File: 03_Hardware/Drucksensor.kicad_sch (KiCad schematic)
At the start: 85 parts, among them J101 24V in, J103 RS485-mini-1, J104 RJ45, J108 RJ45, J109 RJ45, J110 DS18B20, J111 BMP280, J112 RJ45, J113 RS485-mini-1, J114 AVR-ISP-6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

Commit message: Curve Fit Algo auf Spannungsteiler Detektion Sensor geworfen => 18,8k kamen raus. Jetzt wird es mal mit 18k probiert.
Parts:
- R111, R137: value 33k -> 18k
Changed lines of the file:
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@@
       (effects (font (size 1.27 1.27)))
     )
-    (property "Value" "33k" (at 312.42 43.18 90)
+    (property "Value" "18k" (at 312.42 43.18 90)
       (effects (font (size 1.27 1.27)))
     )
@@
       (effects (font (size 1.27 1.27)))
     )
-    (property "Value" "33k" (at 312.42 97.79 90)
-      (effects (font (size 1.27 1.27)))
-    )
+    (property "Value" "18k" (at 312.42 97.79 90)
+      (effects (font (size 1.27 1.27)))
+    )

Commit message: BiDir 5V TVS Diode an ID Leitung Sensor angebracht
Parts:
- added D1, D2: SD05_SOD323, Diode_SMD:D_SOD-323, symbol Diode:SD05_SOD323
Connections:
- net ADC0_ID_1: now also D1.2 (A2)
- net ADC1_ID_2: now also D2.2 (A2)
- net GND: now also D1.1 (A1), D2.1 (A1)
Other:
- note removed: "ESD-Schutz an ID-Widerstandsmessungen fehlen!"
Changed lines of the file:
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@@
   (junction (at 120.65 59.69) (diameter 0) (color 0 0 0 0)
   )
+  (junction (at 317.5 90.17) (diameter 0) (color 0 0 0 0)
+  )
   (junction (at 93.98 36.83) (diameter 0) (color 0 0 0 0)
   )
@@
   (junction (at 276.86 257.81) (diameter 0) (color 0 0 0 0)
   )
+  (junction (at 317.5 35.56) (diameter 0) (color 0 0 0 0)
+  )
   (junction (at 368.3 172.72) (diameter 0) (color 0 0 0 0)
   )
@@
     (stroke (width 0) (type solid))
   )
+  (wire (pts (xy 317.5 87.63) (xy 317.5 90.17))
+    (stroke (width 0) (type default))
+  )
   (wire (pts (xy 119.38 72.39) (xy 120.65 72.39))
     (stroke (width 0) (type default))
@@
     (stroke (width 0) (type solid))
   )
+  (wire (pts (xy 317.5 31.75) (xy 317.5 35.56))
+    (stroke (width 0) (type default))
+  )
   (wire (pts (xy 276.86 234.95) (xy 276.86 245.11))
     (stroke (width 0) (type default))
@@
     (stroke (width 0) (type default))
   )
-  (text "ESD-Schutz an ID-Widerstandsmessungen fehlen!" (at 217.17 77.47 0)
-    (effects (font (size 2.5 2.5) (thickness 0.5) bold (color 221 38 8 1)) (justify left bottom))
-  )
   (text "Messröhre ADC:\nVon Röhre 0-10V\nTeiler 20k:13.895k (33.895k R-ges)\nErgibt Teilerverhältnis von 0,40995\nBei idealem Teilerverhältnis von 0,4096\n"
     (at 361.95 124.46 0)
@@
     )
   )
+  (symbol (lib_id "power:GND") (at 317.5 80.01 0) (mirror x) (unit 1)
+    (in_bom yes) (on_board yes) (dnp no) (fields_autoplaced)
+    (property "Reference" "#PWR01" (at 317.5 73.66 0)
+      (effects (font (size 1.27 1.27)) hide)
+    )
+    (property "Value" "GND" (at 316.865 76.2 90)
+      (effects (font (size 1.27 1.27)) (justify right))
+    )
+    (property "Footprint" "" (at 317.5 80.01 0)
+      (effects (font (size 1.27 1.27)) hide)
+    )
+    (property "Datasheet" "" (at 317.5 80.01 0)
+      (effects (font (size 1.27 1.27)) hide)
+    )
+    (pin "1")
+    (instances
+      (project "Drucksensor"
+        (path "/d772951a-27ae-4d3f-b561-d53c012cef6f"
+          (reference "#PWR01") (unit 1)
+        )
+      )
+    )
+  )
   (symbol (lib_id "power:+5V") (at 165.1 175.26 0) (unit 1)
     (in_bom yes) (on_board yes) (dnp no)
@@
     )
   )
+  (symbol (lib_id "Diode:SD05_SOD323") (at 317.5 27.94 270) (unit 1)
+    (in_bom yes) (on_board yes) (dnp no) (fields_autoplaced)
+    (property "Reference" "D2" (at 322.58 27.94 0)
+      (effects (font (size 1.27 1.27)))
+    )
+    (property "Value" "SD05_SOD323" (at 320.04 27.94 0)
+      (effects (font (size 1.27 1.27)))
+    )
+    (property "Footprint" "Diode_SMD:D_SOD-323" (at 312.42 27.94 0)
+      (effects (font (size 1.27 1.27)) hide)
+    )
+    (property "Datasheet" "https://www.littelfuse.com/~/media/electronics/datasheets/tvs_diode_arrays/littelfuse_tvs_diode_array_sd_c_datasheet.pdf.pdf" (at 317.5 27.94 0)
+      (effects (font (size 1.27 1.27)) hide)
+    )
+    (pin "1")
+    (pin "2")
+    (instances
+      (project "Drucksensor"
+        (path "/d772951a-27ae-4d3f-b561-d53c012cef6f"
+          (reference "D2") (unit 1)
+        )
+      )
+    )
+  )
   (symbol (lib_id "power:+24V") (at 191.77 30.48 90) (mirror x) (unit 1)
     (in_bom yes) (on_board yes) (dnp no)
@@
     )
   )
+  (symbol (lib_id "Diode:SD05_SOD323") (at 317.5 83.82 270) (unit 1)
+    (in_bom yes) (on_board yes) (dnp no) (fields_autoplaced)
+    (property "Reference" "D1" (at 322.58 83.82 0)
+      (effects (font (size 1.27 1.27)))
+    )
+    (property "Value" "SD05_SOD323" (at 320.04 83.82 0)
+      (effects (font (size 1.27 1.27)))
+    )
+    (property "Footprint" "Diode_SMD:D_SOD-323" (at 312.42 83.82 0)
+      (effects (font (size 1.27 1.27)) hide)
+    )
+    (property "Datasheet" "https://www.littelfuse.com/~/media/electronics/datasheets/tvs_diode_arrays/littelfuse_tvs_diode_array_sd_c_datasheet.pdf.pdf" (at 317.5 83.82 0)
+      (effects (font (size 1.27 1.27)) hide)
+    )
+    (pin "1")
+    (pin "2")
+    (instances
+      (project "Drucksensor"
+        (path "/d772951a-27ae-4d3f-b561-d53c012cef6f"
+          (reference "D1") (unit 1)
+        )
+      )
+    )
+  )
   (symbol (lib_id "Device:C") (at 86.36 252.73 0) (unit 1)
     (in_bom yes) (on_board yes) (dnp no) (fields_autoplaced)
@@
         )
       )
+    )
+  )
+  (symbol (lib_id "power:GND") (at 317.5 24.13 0) (mirror x) (unit 1)
+    (in_bom yes) (on_board yes) (dnp no) (fields_autoplaced)
+    (property "Reference" "#PWR02" (at 317.5 17.78 0)
+      (effects (font (size 1.27 1.27)) hide)
+    )
+    (property "Value" "GND" (at 316.865 20.32 90)
+      (effects (font (size 1.27 1.27)) (justify right))
+    )
+    (property "Footprint" "" (at 317.5 24.13 0)
+      (effects (font (size 1.27 1.27)) hide)
+    )
+    (property "Datasheet" "" (at 317.5 24.13 0)
+      (effects (font (size 1.27 1.27)) hide)
+    )
+    (pin "1")
+    (instances
+      (project "Drucksensor"
+        (path "/d772951a-27ae-4d3f-b561-d53c012cef6f"
+          (reference "#PWR02") (unit 1)
+        )
+      )

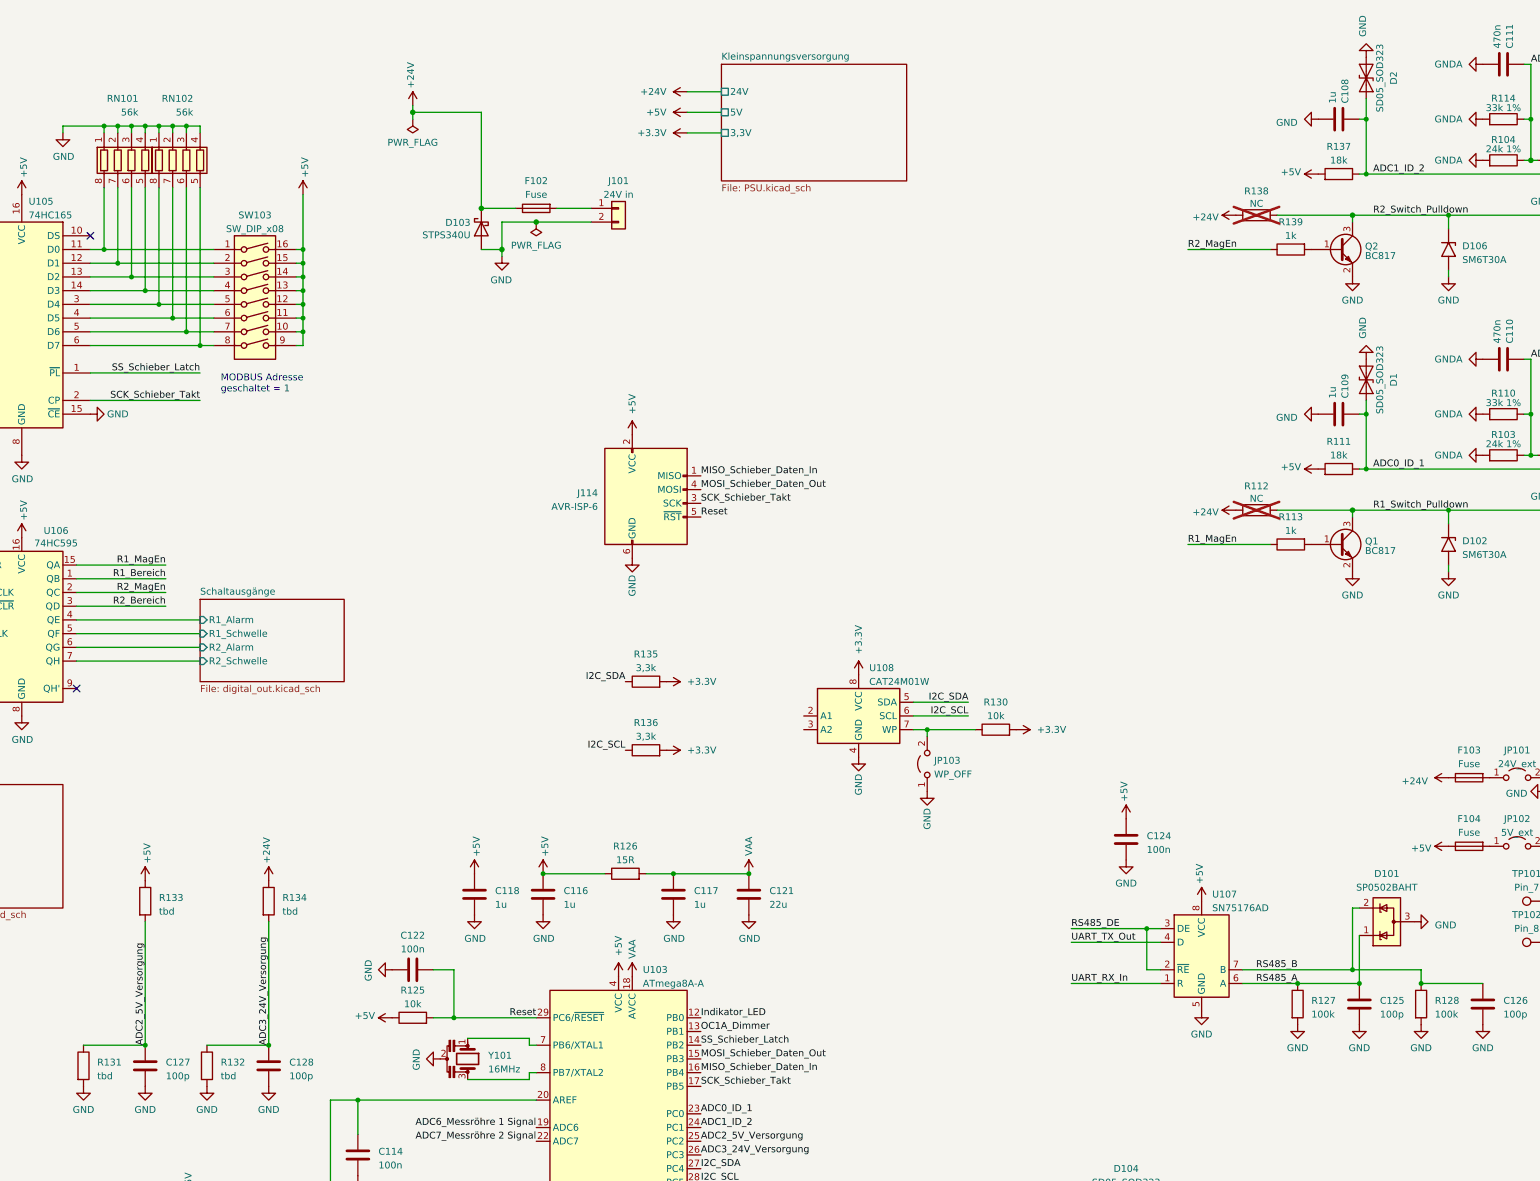
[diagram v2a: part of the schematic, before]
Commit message: Software angefangen - vscode und Platformio, mega328pb
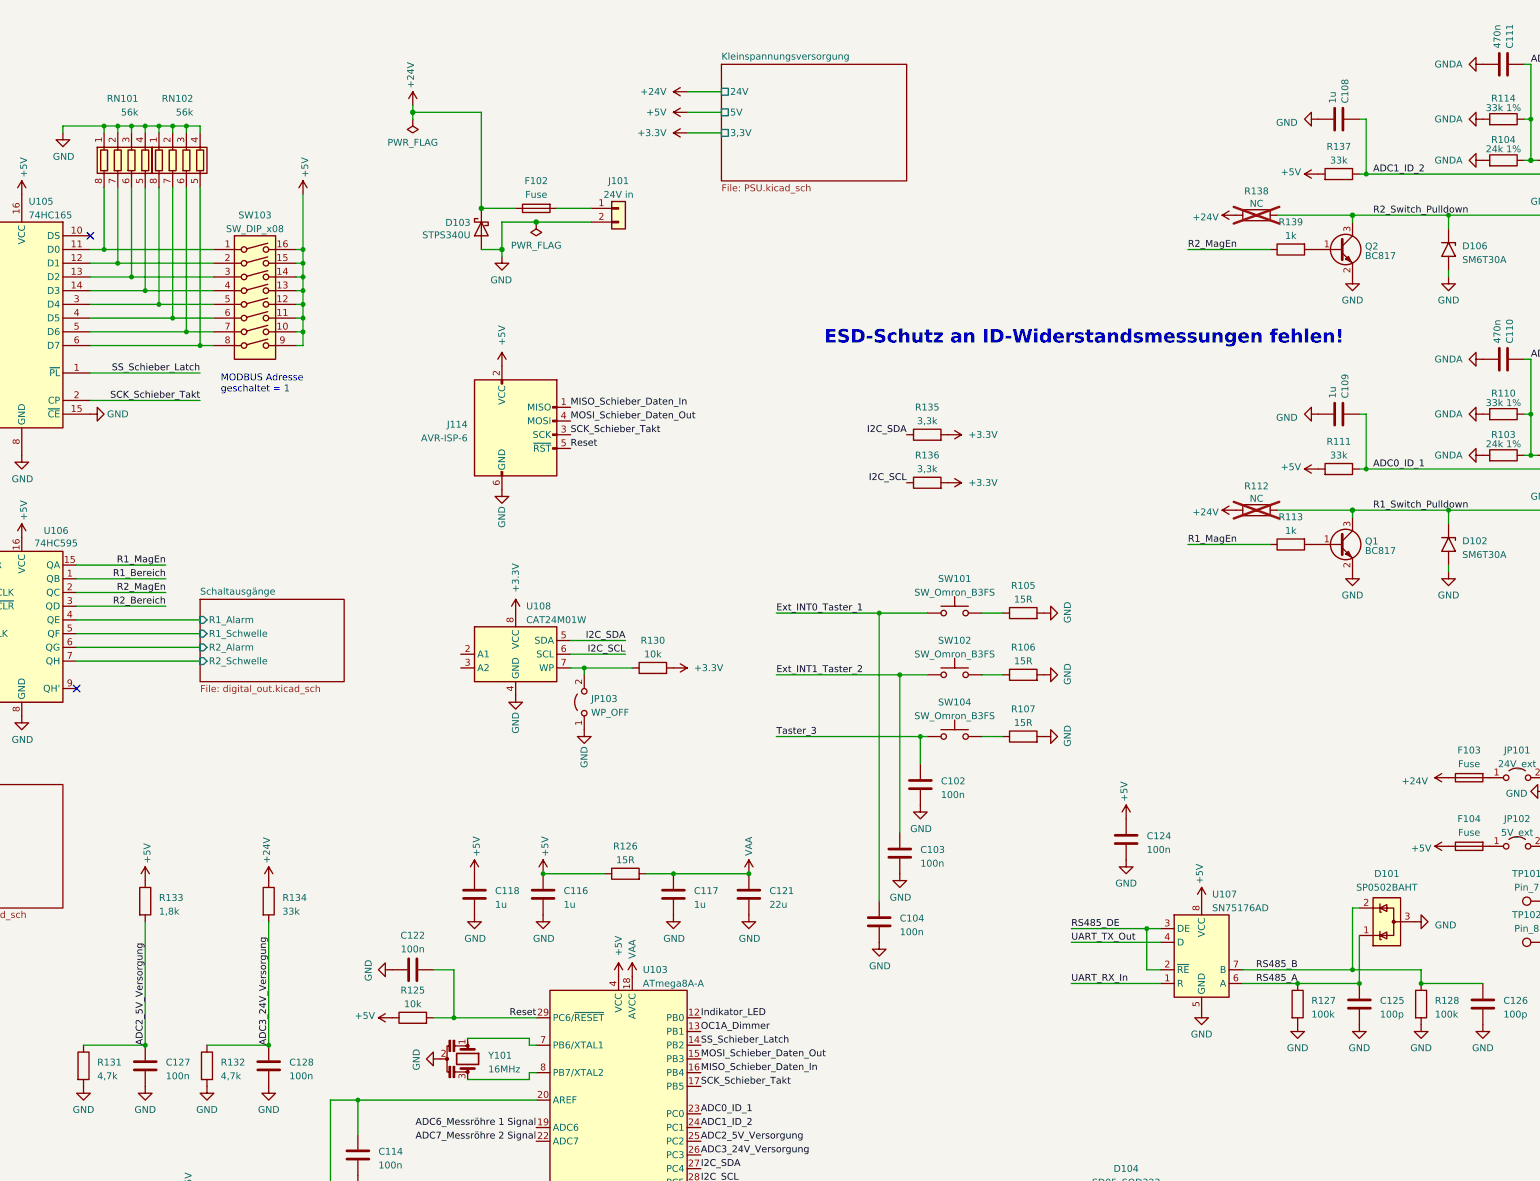
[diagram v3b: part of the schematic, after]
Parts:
- removed D1, D2: SD05_SOD323, Diode_SMD:D_SOD-323, symbol Diode:SD05_SOD323
- added C102, C103, C104: 100n, Capacitor_SMD:C_0603_1608Metric, symbol Device:C
- added R105, R106, R107: 15R, Resistor_SMD:R_0603_1608Metric, symbol Device:R
- added SW101, SW102, SW104: SW_Omron_B3FS, Button_Switch_THT:SW_PUSH-12mm, symbol Switch:SW_Omron_B3FS
- C127, C128: value 100p -> 100n
- R111, R137: value 18k -> 33k
- R131, R132: value tbd -> 4,7k
- R133: value tbd -> 1,8k
- R134: value tbd -> 33k
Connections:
- net Ext_INT0_Taster_1: now also C104.1, SW101.1
- net Ext_INT1_Taster_2: now also C103.1, SW102.1
- net GND: now also C102.2, C103.2, C104.2, R105.2, R106.2, R107.2
- net Taster_3: now also C102.1, SW104.1
- new net: R107.1, SW104.2
- new net: R106.1, SW102.2
- new net: R105.1, SW101.2
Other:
- note added: "ESD-Schutz an ID-Widerstandsmessungen fehlen!"
- moved on the sheet: J114, JP103, R130, R135, R136, U108
